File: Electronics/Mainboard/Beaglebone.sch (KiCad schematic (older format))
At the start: 1 part, among them U15 Beaglebone_Black

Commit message: Reference schematic
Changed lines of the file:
@@
 $Descr A4 11693 8268
 encoding utf-8
-Sheet 3 11
+Sheet 2 11
 Title ""
 Date ""
@@
 Wire Wire Line
 	8450 2500 8300 2500
+Text HLabel 10100 4750 2    50   Output ~ 0
+ADC_CLK
+Text HLabel 10100 4850 2    50   Output ~ 0
+ADC_MOSI
+Text HLabel 10100 4950 2    50   Input ~ 0
+ADC_MISO
+Text HLabel 10100 3650 2    50   Output ~ 0
+DAC_CLK
+Text HLabel 10100 3750 2    50   Output ~ 0
+DAC_MOSI
+Text HLabel 10100 3850 2    50   Input ~ 0
+DAC_MISO
+Text HLabel 10100 3950 2    50   Output ~ 0
+~DAC_LDAC
+Text HLabel 10100 4050 2    50   Output ~ 0
+~DAC_CS-X
+Text HLabel 10100 4150 2    50   Output ~ 0
+~DAC_CS-Y
+Text HLabel 10100 4250 2    50   Output ~ 0
+~DAC_CS-Z
+Text HLabel 10100 4350 2    50   Output ~ 0
+~DAC_CS-Bias
+Text HLabel 10100 5050 2    50   Input ~ 0
+ADC_BUSY
+Text HLabel 10100 5150 2    50   Output ~ 0
+ADC_CONV
 $EndSCHEMATC

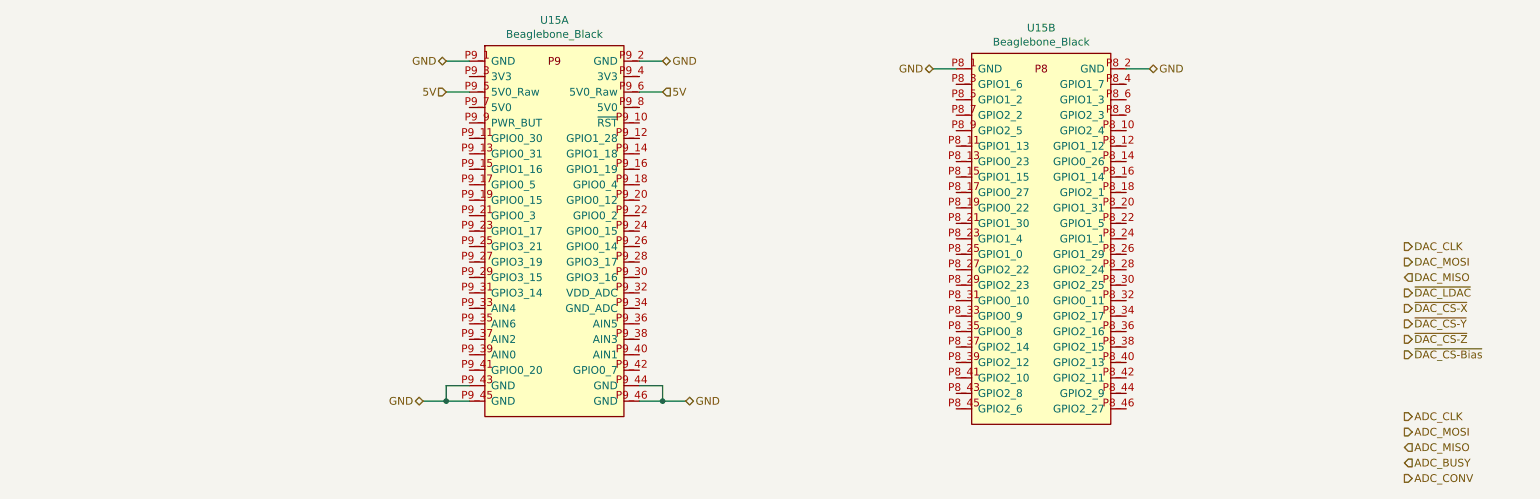
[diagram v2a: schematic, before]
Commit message: SPI Connections finished
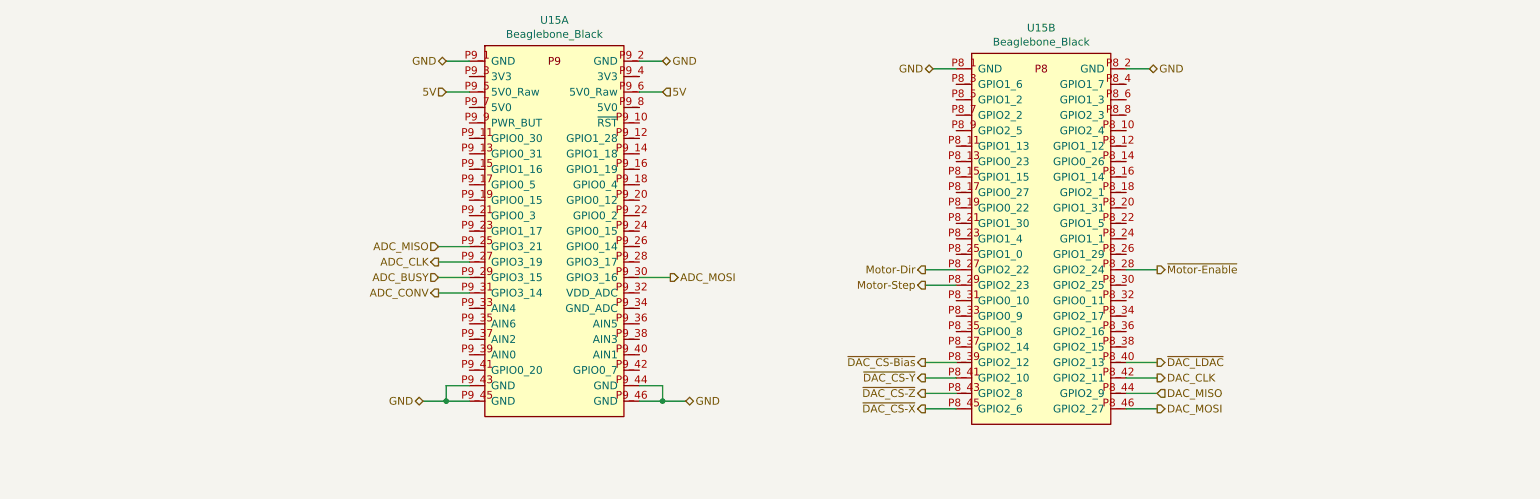
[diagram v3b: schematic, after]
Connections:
- net ADC_BUSY: now also U15.P9_29 (GPIO3_15)
- net ADC_CLK: now also U15.P9_27 (GPIO3_19)
- net ADC_CONV: now also U15.P9_31 (GPIO3_14)
- net ADC_MISO: now also U15.P9_25 (GPIO3_21)
- net ADC_MOSI: now also U15.P9_30 (GPIO3_16)
- net DAC_CLK: now also U15.P8_42 (GPIO2_11)
- net DAC_MISO: now also U15.P8_44 (GPIO2_9)
- net DAC_MOSI: now also U15.P8_46 (GPIO2_27)
- net ~DAC_CS-Bias: now also U15.P8_39 (GPIO2_12)
- net ~DAC_CS-X: now also U15.P8_45 (GPIO2_6)
- net ~DAC_CS-Y: now also U15.P8_41 (GPIO2_10)
- net ~DAC_CS-Z: now also U15.P8_43 (GPIO2_8)
- net ~DAC_LDAC: now also U15.P8_40 (GPIO2_13)
- net Motor-Dir: now reaches U15.P8_27 (GPIO2_22)
- net ~Motor-Enable: now reaches U15.P8_28 (GPIO2_24)
- net Motor-Step: now reaches U15.P8_29 (GPIO2_23)
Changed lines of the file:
@@
 Wire Wire Line
 	8450 2500 8300 2500
-Text HLabel 10100 4750 2    50   Output ~ 0
+Text HLabel 3850 3750 0    50   Output ~ 0
 ADC_CLK
-Text HLabel 10100 4850 2    50   Output ~ 0
+Text HLabel 5350 3850 2    50   Output ~ 0
 ADC_MOSI
-Text HLabel 10100 4950 2    50   Input ~ 0
+Text HLabel 3850 3650 0    50   Input ~ 0
 ADC_MISO
-Text HLabel 10100 3650 2    50   Output ~ 0
+Text HLabel 8500 4500 2    50   Output ~ 0
 DAC_CLK
-Text HLabel 10100 3750 2    50   Output ~ 0
+Text HLabel 8500 4700 2    50   Output ~ 0
 DAC_MOSI
-Text HLabel 10100 3850 2    50   Input ~ 0
+Text HLabel 8500 4600 2    50   Input ~ 0
 DAC_MISO
-Text HLabel 10100 3950 2    50   Output ~ 0
+Text HLabel 8500 4400 2    50   Output ~ 0
 ~DAC_LDAC
-Text HLabel 10100 4050 2    50   Output ~ 0
+Text HLabel 7000 4700 0    50   Output ~ 0
 ~DAC_CS-X
-Text HLabel 10100 4150 2    50   Output ~ 0
+Text HLabel 7000 4500 0    50   Output ~ 0
 ~DAC_CS-Y
-Text HLabel 10100 4250 2    50   Output ~ 0
+Text HLabel 7000 4600 0    50   Output ~ 0
 ~DAC_CS-Z
-Text HLabel 10100 4350 2    50   Output ~ 0
+Text HLabel 7000 4400 0    50   Output ~ 0
 ~DAC_CS-Bias
-Text HLabel 10100 5050 2    50   Input ~ 0
+Text HLabel 3850 3850 0    50   Input ~ 0
 ADC_BUSY
-Text HLabel 10100 5150 2    50   Output ~ 0
+Text HLabel 3850 3950 0    50   Output ~ 0
 ADC_CONV
+Wire Wire Line
+	7200 4700 7000 4700
+Wire Wire Line
+	8500 4600 8300 4600
+Wire Wire Line
+	8500 4700 8300 4700
+Wire Wire Line
+	8500 4400 8300 4400
+Wire Wire Line
+	8500 4500 8300 4500
+Wire Wire Line
+	7000 4400 7200 4400
+Wire Wire Line
+	7000 4500 7200 4500
+Wire Wire Line
+	7000 4600 7200 4600
+Text HLabel 8500 3800 2    50   Output ~ 0
+~Motor-Enable
+Text HLabel 7000 3800 0    50   Output ~ 0
+Motor-Dir
+Text HLabel 7000 3900 0    50   Output ~ 0
+Motor-Step
+Wire Wire Line
+	8500 3800 8300 3800
+Wire Wire Line
+	7000 3900 7200 3900
+Wire Wire Line
+	7000 3800 7200 3800
+Wire Wire Line
+	3850 3650 4050 3650
+Wire Wire Line
+	3850 3750 4050 3750
+Wire Wire Line
+	3850 3850 4050 3850
+Wire Wire Line
+	3850 3950 4050 3950
+Wire Wire Line
+	5350 3850 5150 3850
 $EndSCHEMATC

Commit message: Layout nearly finished
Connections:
- net SCL: now reaches U15.P9_19 (GPIO0_15)
- net SDA: now reaches U15.P9_20 (GPIO0_12)
- net 3V3: now reaches U15.P9_3 (3V3)
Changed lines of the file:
@@
 Wire Wire Line
 	5350 3850 5150 3850
+Text HLabel 3900 2550 0    50   Output ~ 0
+3V3
+Wire Wire Line
+	3900 2550 4050 2550
+Text HLabel 5350 3350 2    50   BiDi ~ 0
+SDA
+Text HLabel 3850 3350 0    50   Output ~ 0
+SCL
+Wire Wire Line
+	3850 3350 4050 3350
+Wire Wire Line
+	5350 3350 5150 3350
 $EndSCHEMATC

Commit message: Mainboard layout and schematic done
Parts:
- added JP1, JP13, JP14, JP15, JP16, JP17, JP18, JP19, JP2, JP20, JP21, JP22, JP23, JP24, JP25, JP26, JP27, JP28: Jumper, Jumper:SolderJumper-2_P1.3mm_Bridged_RoundedPad1.0x1.5mm, symbol Device:Jumper
- added TP17, TP18, TP19, TP20, TP21, TP22, TP23, TP24, TP25, TP26, TP27, TP28, TP29, TP30, TP31, TP32, TP33, TP34, TP35, TP36, TP37, TP38, TP39, TP40, TP41, TP42, TP43, TP44, TP45, TP46, TP47, TP48, TP49, TP50, TP51, TP52, TP53, TP54, TP55, TP56, TP57, TP58, TP59, TP60, TP61, TP62, TP63, TP64, TP65, TP66, TP67, TP68, TP69, TP70, TP71, TP73, TP74, TP75, TP76: TestPoint, TestPoint:TestPoint_Pad_D1.5mm, symbol Connector:TestPoint
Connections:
- net ADC_BUSY: now also JP13.1; no longer U15.P9_29 (GPIO3_15)
- net ADC_CLK: now also JP2.1; no longer U15.P9_27 (GPIO3_19)
- net ADC_CONV: now also JP14.1; no longer U15.P9_31 (GPIO3_14)
- net ADC_MISO: now also JP1.1; no longer U15.P9_25 (GPIO3_21)
- net ADC_MOSI: now also JP15.2; no longer U15.P9_30 (GPIO3_16)
- net DAC_CLK: now also JP24.2; no longer U15.P8_42 (GPIO2_11)
- net DAC_MISO: now also JP25.2; no longer U15.P8_44 (GPIO2_9)
- net DAC_MOSI: now also JP26.2; no longer U15.P8_46 (GPIO2_27)
- net Motor-Dir: now also JP16.1; no longer U15.P8_27 (GPIO2_22)
- net Motor-Step: now also JP17.1; no longer U15.P8_29 (GPIO2_23)
- net SCL: now also JP27.1; no longer U15.P9_19 (GPIO0_15)
- net SDA: now also JP28.2; no longer U15.P9_20 (GPIO0_12)
- net ~DAC_CS-Bias: now also JP18.1; no longer U15.P8_39 (GPIO2_12)
- net ~DAC_CS-X: now also JP21.1; no longer U15.P8_45 (GPIO2_6)
- net ~DAC_CS-Y: now also JP19.1; no longer U15.P8_41 (GPIO2_10)
- net ~DAC_CS-Z: now also JP20.1; no longer U15.P8_43 (GPIO2_8)
- net ~DAC_LDAC: now also JP23.2; no longer U15.P8_40 (GPIO2_13)
- net ~Motor-Enable: now also JP22.2; no longer U15.P8_28 (GPIO2_24)
- net at U15.P9_10 (~RST): now also TP29.1
- net at U15.P9_11 (GPIO0_30): now also TP18.1
- net at U15.P9_12 (GPIO1_28): now also TP30.1
- net at U15.P9_13 (GPIO0_31): now also TP19.1
- net at U15.P9_14 (GPIO1_18): now also TP31.1
- net at U15.P9_15 (GPIO1_16): now also TP20.1
- net at U15.P9_16 (GPIO1_19): now also TP32.1
- net at U15.P9_17 (GPIO0_5): now also TP21.1
- net at U15.P9_18 (GPIO0_4): now also TP33.1
- net at U15.P9_21 (GPIO0_3): now also TP22.1
- net at U15.P9_22 (GPIO0_2): now also TP34.1
- net at U15.P9_23 (GPIO1_17): now also TP23.1
- net at U15.P9_24 (GPIO0_15): now also TP35.1
- net at U15.P9_26 (GPIO0_14): now also TP36.1
- net at U15.P9_28 (GPIO3_17): now also TP37.1
- net at U15.P9_32 (VDD_ADC): now also TP38.1
- net at U15.P9_33 (AIN4): now also TP24.1
- net at U15.P9_34 (GND_ADC): now also TP39.1
- net at U15.P9_35 (AIN6): now also TP25.1
- net at U15.P9_36 (AIN5): now also TP40.1
- net at U15.P9_37 (AIN2): now also TP26.1
- net at U15.P9_38 (AIN3): now also TP41.1
- net at U15.P9_39 (AIN0): now also TP27.1
- net at U15.P9_40 (AIN1): now also TP42.1
- net at U15.P9_41 (GPIO0_20): now also TP28.1
- net at U15.P9_42 (GPIO0_7): now also TP43.1
- net at U15.P9_8 (5V0): now also TP56.1
- net at U15.P9_9 (PWR_BUT): now also TP17.1
- net at U15.P8_10 (GPIO2_4): now also TP63.1
- net at U15.P8_11 (GPIO1_13): now also TP48.1
- net at U15.P8_12 (GPIO1_12): now also TP64.1
- net at U15.P8_13 (GPIO0_23): now also TP49.1
- net at U15.P8_14 (GPIO0_26): now also TP65.1
- net at U15.P8_15 (GPIO1_15): now also TP50.1
- net at U15.P8_16 (GPIO1_14): now also TP66.1
- net at U15.P8_17 (GPIO0_27): now also TP51.1
- net at U15.P8_18 (GPIO2_1): now also TP67.1
- net at U15.P8_19 (GPIO0_22): now also TP52.1
- net at U15.P8_20 (GPIO1_31): now also TP68.1
- net at U15.P8_21 (GPIO1_30): now also TP53.1
- net at U15.P8_22 (GPIO1_5): now also TP69.1
- net at U15.P8_23 (GPIO1_4): now also TP54.1
- net at U15.P8_24 (GPIO1_1): now also TP70.1
- net at U15.P8_25 (GPIO1_0): now also TP55.1
- net at U15.P8_26 (GPIO1_29): now also TP71.1
- net at U15.P8_3 (GPIO1_6): now also TP44.1
- net at U15.P8_32 (GPIO0_11): now also TP73.1
- net at U15.P8_33 (GPIO0_9): now also TP57.1
- net at U15.P8_34 (GPIO2_17): now also TP74.1
- net at U15.P8_35 (GPIO0_8): now also TP58.1
- net at U15.P8_36 (GPIO2_16): now also TP75.1
- net at U15.P8_37 (GPIO2_14): now also TP59.1
- net at U15.P8_38 (GPIO2_15): now also TP76.1
- net at U15.P8_4 (GPIO1_7): now also TP60.1
- net at U15.P8_5 (GPIO1_2): now also TP45.1
- net at U15.P8_6 (GPIO1_3): now also TP61.1
- net at U15.P8_7 (GPIO2_2): now also TP46.1
- net at U15.P8_8 (GPIO2_3): now also TP62.1
- net at U15.P8_9 (GPIO2_5): now also TP47.1
- new net: JP27.2, U15.P9_19 (GPIO0_15)
- new net: JP28.1, U15.P9_20 (GPIO0_12)
- new net: JP1.2, U15.P9_25 (GPIO3_21)
- new net: JP2.2, U15.P9_27 (GPIO3_19)
- new net: JP13.2, U15.P9_29 (GPIO3_15)
- new net: JP15.1, U15.P9_30 (GPIO3_16)
- new net: JP14.2, U15.P9_31 (GPIO3_14)
- new net: JP16.2, U15.P8_27 (GPIO2_22)
- new net: JP22.1, U15.P8_28 (GPIO2_24)
- new net: JP17.2, U15.P8_29 (GPIO2_23)
- new net: JP18.2, U15.P8_39 (GPIO2_12)
- new net: JP23.1, U15.P8_40 (GPIO2_13)
- new net: JP19.2, U15.P8_41 (GPIO2_10)
- new net: JP24.1, U15.P8_42 (GPIO2_11)
- new net: JP20.2, U15.P8_43 (GPIO2_8)
- new net: JP25.1, U15.P8_44 (GPIO2_9)
- new net: JP21.2, U15.P8_45 (GPIO2_6)
- new net: JP26.1, U15.P8_46 (GPIO2_27)
- no-connect marks 0 -> 2
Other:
- moved on the sheet: U15A
